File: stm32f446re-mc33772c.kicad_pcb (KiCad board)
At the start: 4 copper layers, 90.9 x 61.3 mm, 123 parts, among them J1 Conn_01x02, J2 USB_B_Micro, J3 Conn_01x03, J4 Conn_01x03, J5 S7B-XH-A, J6 SM06B-GHS-TB, U1 STM32F446RET6, U2 MC33772CTP1AE, U3 LD1086D2M33TR, U4 AMS1117-3.3, U6 LMR51450SDRRR, U7 SN65HVD232, Y1 16MHz

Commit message: fix: VCAP_1 4.7uF, In1.Cu fill GND
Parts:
- added C62: 4.7u, Capacitor_SMD:C_0402_1005Metric, F.Cu at (178.5, 88.0)
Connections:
- U1 pad 30: unconnected-(U1-VCAP_1-Pad30) -> Net-(U1-VCAP_1)
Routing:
- net Net-(U1-VCAP_1): track 0.00 -> 2.51 mm
- net Rsense_P: track 210.1 -> 211.1 mm, vias 55 -> 56
- added copper zone on In1.Cu, net Rsense_P

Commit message: update silkscreen, make 6pin closer to edge
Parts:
- moved J6 1.11 mm to (217.5, 82.8)
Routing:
- net CANH: track 12.5 -> 13.6 mm
- net Buck_5V: track 72.6 -> 73.7 mm
- net CANL: track 15.5 -> 16.6 mm
- net Rsense_P: track 211.1 -> 212.2 mm
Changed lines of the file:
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@@
 	(footprint "MyFootLib:JST_SM06B-GHS-TB"
 		(layer "F.Cu")
-		(at 216.386997 82.813562 90)
+		(at 217.5 82.813562 90)
 		(property "Reference" "J6"
 			(at 7.225 0.925 90)
@@
 		(layer "Edge.Cuts")
 	)
-	(gr_text "LDO_3v3"
-		(at 212.299937 62.515263 0)
+	(gr_text "BAT"
+		(at 210.560055 57.352354 90)
 		(layer "F.SilkS")
 		(effects
@@
 		)
 	)
-	(gr_text "BAT"
-		(at 210.560055 57.352354 90)
+	(gr_text "LDO_3v3"
+		(at 213 65.5 90)
 		(layer "F.SilkS")
 		(effects
@@
 	)
 	(segment
-		(start 214.511997 79.688562)
-		(end 214.511997 80.938562)
+		(start 215.625 79.688562)
+		(end 215.625 80.938562)
 		(width 1)
 		(layer "F.Cu")
@@
 	)
 	(segment
-		(start 214.511997 79.688562)
-		(end 212.411997 79.688562)
-		(width 1)
-		(layer "F.Cu")
-		(net "Rsense_P")
-	)
-	(segment
 		(start 179.825 69.9)
 		(end 179.825 70.7)
@@
 	)
 	(segment
+		(start 215.625 79.688562)
+		(end 212.411997 79.688562)
+		(width 1)
+		(layer "F.Cu")
+		(net "Rsense_P")
+	)
+	(segment
 		(start 196.9133 81.4048)
 		(end 197.4785 81.97)
@@
 	)
 	(segment
-		(start 208.748938 83.438562)
-		(end 214.511997 83.438562)
+		(start 208 84.1875)
+		(end 208.748938 83.438562)
 		(width 0.2)
 		(layer "F.Cu")
@@
 	)
 	(segment
-		(start 208 84.1875)
-		(end 208.748938 83.438562)
+		(start 208.748938 83.438562)
+		(end 215.625 83.438562)
 		(width 0.2)
 		(layer "F.Cu")
@@
 	(segment
 		(start 208.926062 82.188562)
-		(end 214.511997 82.188562)
+		(end 215.625 82.188562)
 		(width 0.2)
 		(layer "F.Cu")
@@
 	)
 	(segment
-		(start 208 81.2625)
-		(end 208.926062 82.188562)
+		(start 207.9274 81.3351)
+		(end 208 81.2625)
 		(width 0.2)
 		(layer "F.Cu")
@@
 	)
 	(segment
-		(start 207.9274 81.3351)
-		(end 208 81.2625)
+		(start 202.2202 81.3351)
+		(end 207.9274 81.3351)
 		(width 0.2)
 		(layer "F.Cu")
@@
 	)
 	(segment
-		(start 202.2202 81.3351)
-		(end 207.9274 81.3351)
+		(start 208 81.2625)
+		(end 208.926062 82.188562)
 		(width 0.2)
 		(layer "F.Cu")
@@
 	)
 	(segment
-		(start 214.511997 85.938562)
-		(end 214.511997 84.688562)
+		(start 215.625 85.938562)
+		(end 215.625 84.688562)
 		(width 1)
 		(layer "F.Cu")
@@
 	)
 	(segment
+		(start 212.451997 85.938562)
+		(end 215.625 85.938562)
+		(width 1)
+		(layer "F.Cu")
+		(net "Buck_5V")
+	)
+	(segment
 		(start 196.6 53.45)
 		(end 198.2 51.85)
@@
 		(width 1)
 		(layer "F.Cu")
-		(net "Buck_5V")
-	)
-	(segment
-		(start 212.451997 85.938562)
-		(end 214.511997 85.938562)
-		(width 1)
-		(layer "F.Cu")

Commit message: change crystal from 16MHz to 8MHz
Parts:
- C2, C3: value 8p -> 12p
- Y1: value 16MHz -> 8MHz; footprint Crystal:Crystal_SMD_Abracon_ABM8AIG-4Pin_3.2x2.5mm -> Crystal:Crystal_SMD_3225-4Pin_3.2x2.5mm
- moved C3 0.71 mm to (189.0, 73.5), turned to 90 degrees
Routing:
- net Rsense_P: track 212.2 -> 208.8 mm, vias 56 -> 55
- net LDO_3.3V: track 133.1 -> 131.3 mm
- net Net-(U1-PH1): track 14.3 -> 12.7 mm

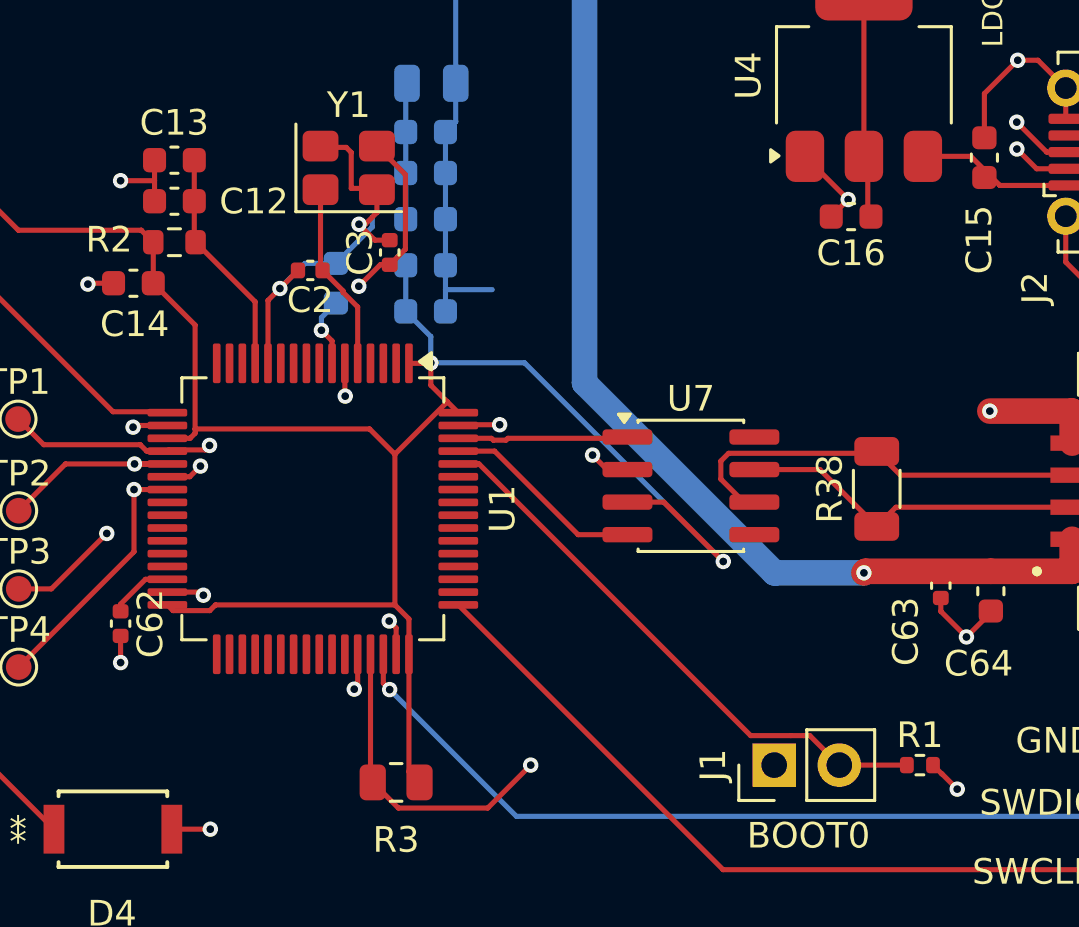
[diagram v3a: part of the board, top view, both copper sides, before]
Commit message: add USB OTG FS VBUS sensing
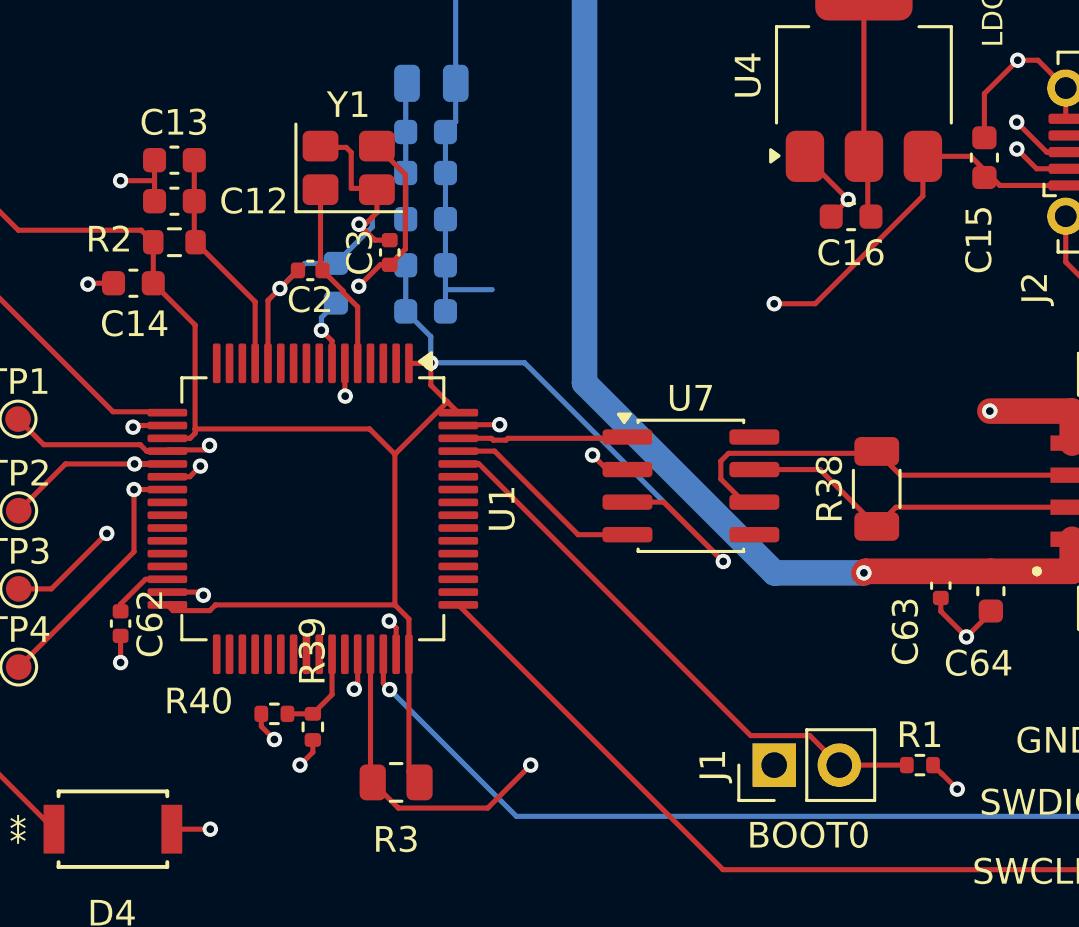
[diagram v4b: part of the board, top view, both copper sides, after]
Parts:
- added R39: 10k, Resistor_SMD:R_0402_1005Metric, F.Cu at (186.0, 92.0)
- added R40: 4.7k, Resistor_SMD:R_0402_1005Metric, F.Cu at (184.5, 91.5)
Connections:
- U1 pad 42: unconnected-(U1-PA9-Pad42) -> Net-(U1-PA9)
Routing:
- net VBUS_5V: track 6.04 -> 44.4 mm, vias 0 -> 2
- net Net-(U1-PA9): track 0.00 -> 3.63 mm
- net Rsense_P: track 208.8 -> 210.0 mm, vias 55 -> 56

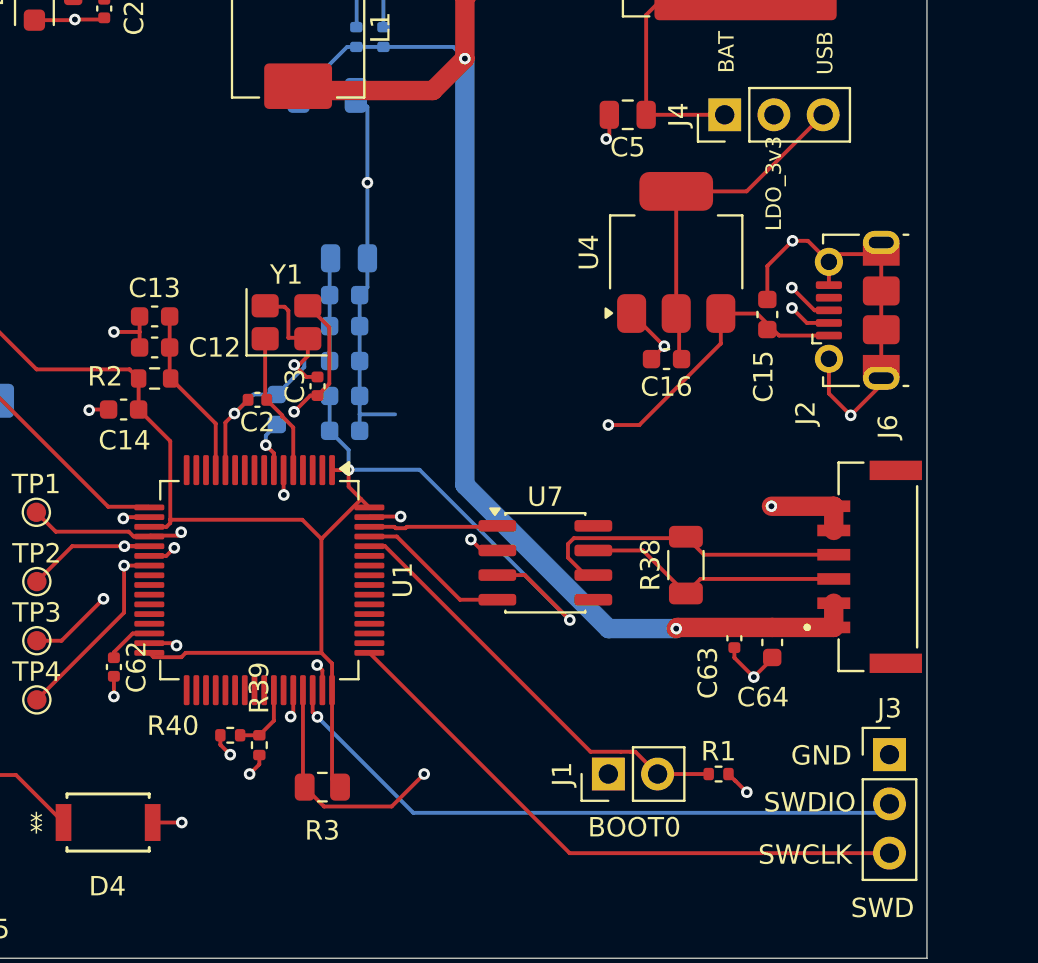
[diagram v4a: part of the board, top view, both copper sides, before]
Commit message: remove DRC error/warning
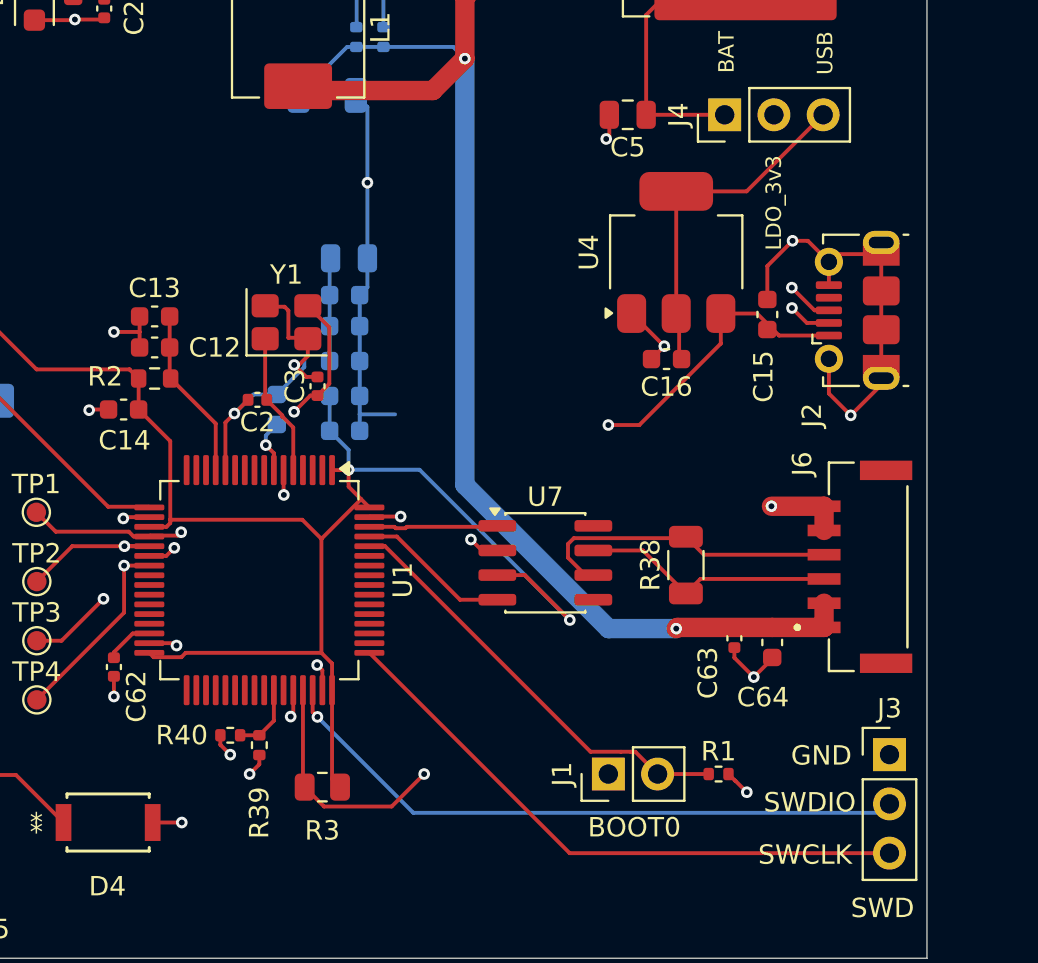
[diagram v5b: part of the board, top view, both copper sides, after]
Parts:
- moved J6 0.50 mm to (217.0, 82.8)
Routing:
- net Rsense_P: track 210.0 -> 209.5 mm
- net CANL: track 16.6 -> 16.1 mm
- net CANH: track 13.6 -> 13.1 mm
- net Buck_5V: track 73.7 -> 73.2 mm
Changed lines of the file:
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@@
 		(tags "Micro-USB SMD Typ-B")
 		(property "Reference" "J2"
-			(at -5.29904 -2.660917 90)
+			(at -5.414951 -2.336815 90)
 			(layer "F.SilkS")
 			(effects
@@
 	(footprint "MyFootLib:JST_SM06B-GHS-TB"
 		(layer "F.Cu")
-		(at 217.5 82.813562 90)
+		(at 217 82.813562 90)
 		(property "Reference" "J6"
-			(at 7.225 0.925 90)
+			(at 5.313562 -3 90)
 			(layer "F.SilkS")
 			(effects
@@
 		(tags "resistor")
 		(property "Reference" "R39"
-			(at -2.955 0.005 90)
+			(at 3.49 0 90)
 			(layer "F.SilkS")
 			(effects
@@
 		(tags "capacitor")
 		(property "Reference" "C62"
-			(at 0 -1.16 90)
+			(at 1.52 -1.16 90)
 			(layer "F.SilkS")
 			(effects
@@
 		(tags "resistor")
 		(property "Reference" "R40"
-			(at -2.955 -0.485 0)
+			(at -2.5 0 0)
 			(layer "F.SilkS")
 			(effects
@@
 	)
 	(gr_text "LDO_3v3"
-		(at 213 65.5 90)
+		(at 213 66.5 90)
 		(layer "F.SilkS")
 		(effects
@@
 	)
 	(segment
-		(start 215.625 79.688562)
-		(end 215.625 80.938562)
+		(start 215.125 79.688562)
+		(end 215.125 80.938562)
 		(width 1)
 		(layer "F.Cu")
@@
 	)
 	(segment
+		(start 215.125 79.688562)
+		(end 212.411997 79.688562)
+		(width 1)
+		(layer "F.Cu")
+		(net "Rsense_P")
+	)
+	(segment
 		(start 168.6995 67.68)
 		(end 168.6 67.68)
@@
 	)
 	(segment
-		(start 215.625 79.688562)
-		(end 212.411997 79.688562)
-		(width 1)
-		(layer "F.Cu")
-		(net "Rsense_P")
-	)
-	(segment
 		(start 196.9133 81.4048)
 		(end 197.4785 81.97)
@@
 	)
 	(segment
-		(start 203.225 81.97)
-		(end 205.7825 81.97)
+		(start 208.748938 83.438562)
+		(end 215.125 83.438562)
 		(width 0.2)
 		(layer "F.Cu")
@@
 	)
 	(segment
-		(start 208 84.1875)
-		(end 208.748938 83.438562)
+		(start 203.225 81.97)
+		(end 205.7825 81.97)
 		(width 0.2)
 		(layer "F.Cu")
@@
 	)
 	(segment
-		(start 208.748938 83.438562)
-		(end 215.625 83.438562)
+		(start 208 84.1875)
+		(end 208.748938 83.438562)
 		(width 0.2)
 		(layer "F.Cu")
@@
 	)
 	(segment
+		(start 208.926062 82.188562)
+		(end 215.125 82.188562)
+		(width 0.2)
+		(layer "F.Cu")
+		(net "CANL")
+	)
+	(segment
 		(start 201.9183 81.637)
 		(end 202.2202 81.3351)
@@
 	)
 	(segment
-		(start 203.225 83.24)
-		(end 202.8167 83.24)
+		(start 208 81.2625)
+		(end 208.926062 82.188562)
 		(width 0.2)
 		(layer "F.Cu")
@@
 	)
 	(segment
-		(start 208.926062 82.188562)
-		(end 215.625 82.188562)
+		(start 203.225 83.24)
+		(end 202.8167 83.24)
 		(width 0.2)
 		(layer "F.Cu")
@@
 	)
 	(segment
-		(start 208 81.2625)
-		(end 208.926062 82.188562)
-		(width 0.2)
-		(layer "F.Cu")
-		(net "CANL")
-	)
-	(segment
 		(start 187.75 77.825)
 		(end 187.75 75.6263)
@@
 	)
 	(segment
-		(start 215.625 85.938562)
-		(end 215.625 84.688562)
+		(start 215.125 85.938562)
+		(end 215.125 84.688562)
 		(width 1)
 		(layer "F.Cu")
@@
 	(segment
 		(start 212.451997 85.938562)
-		(end 215.625 85.938562)
+		(end 215.125 85.938562)
 		(width 1)
 		(layer "F.Cu")
